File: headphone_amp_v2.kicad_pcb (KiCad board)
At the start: 2 copper layers, 94 x 73.7 mm, 73 parts, among them J1 USB_OTG, J2 HID_JMP, J3 AudioJack3_Ground, U1 PCM2707PJTG4, U2 PCM1794A, U3 TPS60501DGS, U4 OPA2134PA, U5 OPA2134PA, U6 LM2662M, Y1 12Mhz

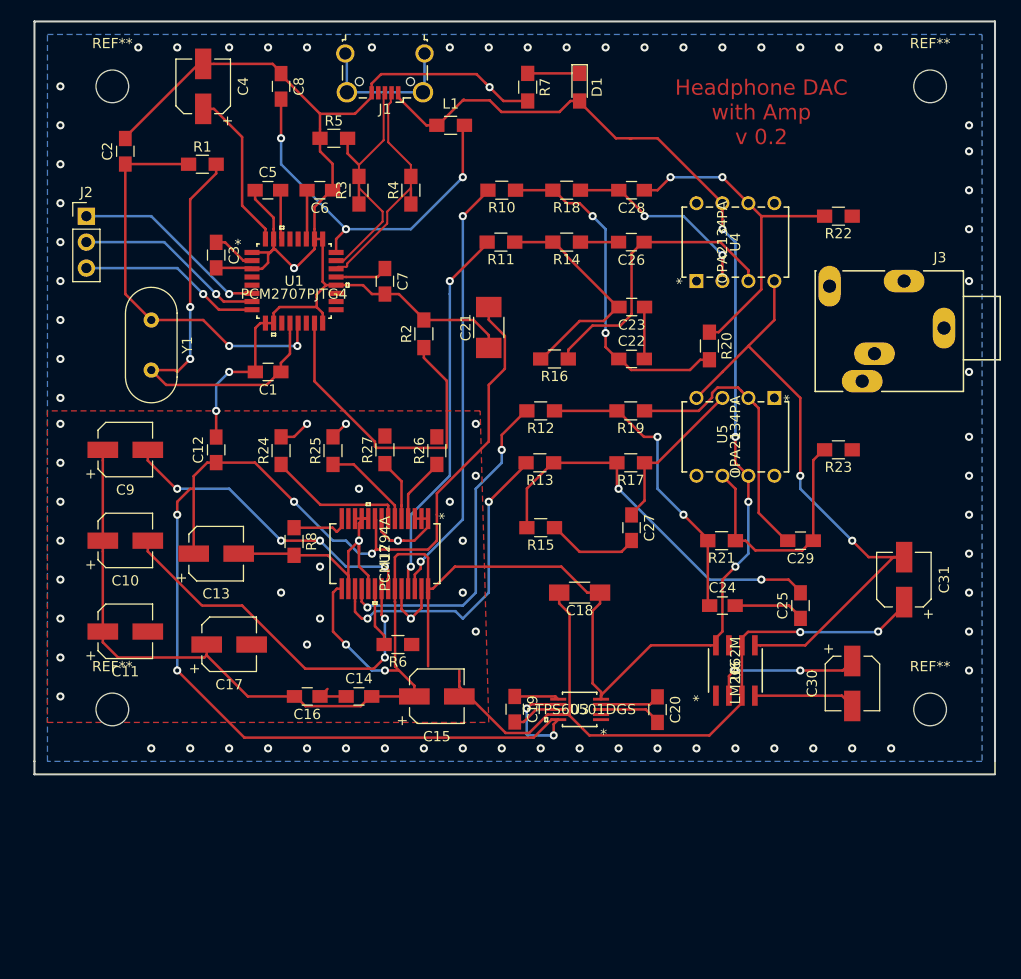
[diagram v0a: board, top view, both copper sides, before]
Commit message: updated the layout of components and rerouted the traces. The components are grouped more nicely, the board length was reduced by 5mm
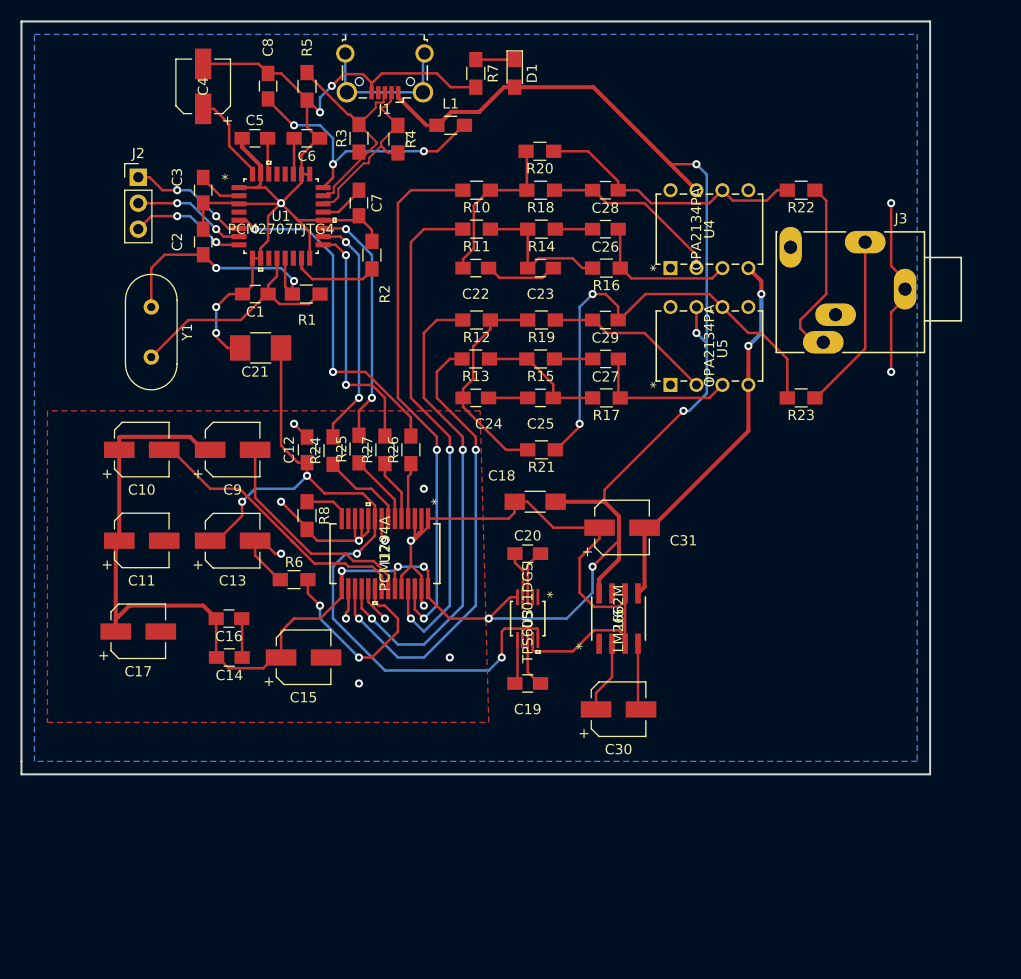
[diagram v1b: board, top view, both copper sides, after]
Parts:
- removed REF** (x4): MountingHole_3.2mm_M3, Mounting_Holes:MountingHole_3.2mm_M3
- moved C25 32.6 mm to (72.4, 49.5), turned to 0 degrees
- moved C24 31.5 mm to (66.0, 49.5)
- moved C29 28.8 mm to (78.7, 41.9)
- moved C31 28.1 mm to (80.3, 62.2), turned to 0 degrees
- moved R20 25.3 mm to (72.3, 25.4), turned to 180 degrees
- moved C30 23.0 mm to (80.0, 80.0), turned to 0 degrees
- moved C21 22.4 mm to (45.0, 44.6), turned to 0 degrees
- moved C20 19.9 mm to (71.1, 64.8), turned to 0 degrees
- moved R21 19.7 mm to (72.5, 54.6)
- moved C22 17.6 mm to (66.0, 36.8)
- moved U5 17.3 mm to (92.7, 40.6), turned to 90 degrees
- moved C27 16.7 mm to (78.7, 45.7), turned to 180 degrees
- moved R15 16.5 mm to (72.4, 45.7)
- moved R1 16.3 mm to (49.5, 39.4)
- moved C15 13.6 mm to (49.2, 74.9)
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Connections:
- net BCK renamed CLK_N
- net DATA renamed DATA_P
- net LRCK renamed DATA_N
- net SCK renamed CLK_P
- J3 pad 1: (no net) -> OUTR
- J3 pad 2: (no net) -> OUTL
- J3 pad 3: (no net) -> GND
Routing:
- net 3.3V: track 135.0 -> 75.7 mm, vias 6 -> 4
- net DATA_N: track 0.00 -> 33.5 mm, vias 0 -> 2
- net Net-(C25-Pad2): track 38.4 -> 12.4 mm, vias 2 -> 0
- net GND: track 252.4 -> 227.3 mm, vias 87 -> 19
- net -5V: track 61.8 -> 37.8 mm
- net DATA_P: track 0.00 -> 23.4 mm, vias 0 -> 2
- net Net-(R2-Pad1): track 32.3 -> 8.98 mm
- net CLK_N: track 1.80 -> 25.0 mm, vias 1 -> 2
- net 5V: track 223.9 -> 201.9 mm, vias 6 -> 8
- net Net-(C29-Pad1): track 24.7 -> 45.2 mm, vias 0 -> 2
- net CLK_P: track 3.07 -> 23.1 mm, vias 1 -> 2
- net Net-(C1-Pad1): track 43.5 -> 23.7 mm, vias 2 -> 0
- net OUTL: track 0.00 -> 17.9 mm
- net OUTR: track 0.00 -> 17.3 mm
- net Net-(C22-Pad1): track 33.4 -> 16.2 mm, vias 2 -> 0
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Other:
- board size 94 x 73.7 mm -> 88.9 x 73.7 mm
- board text removed: "Headphone DAC with Amp v 0.2"

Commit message: added mountingholes(m3)
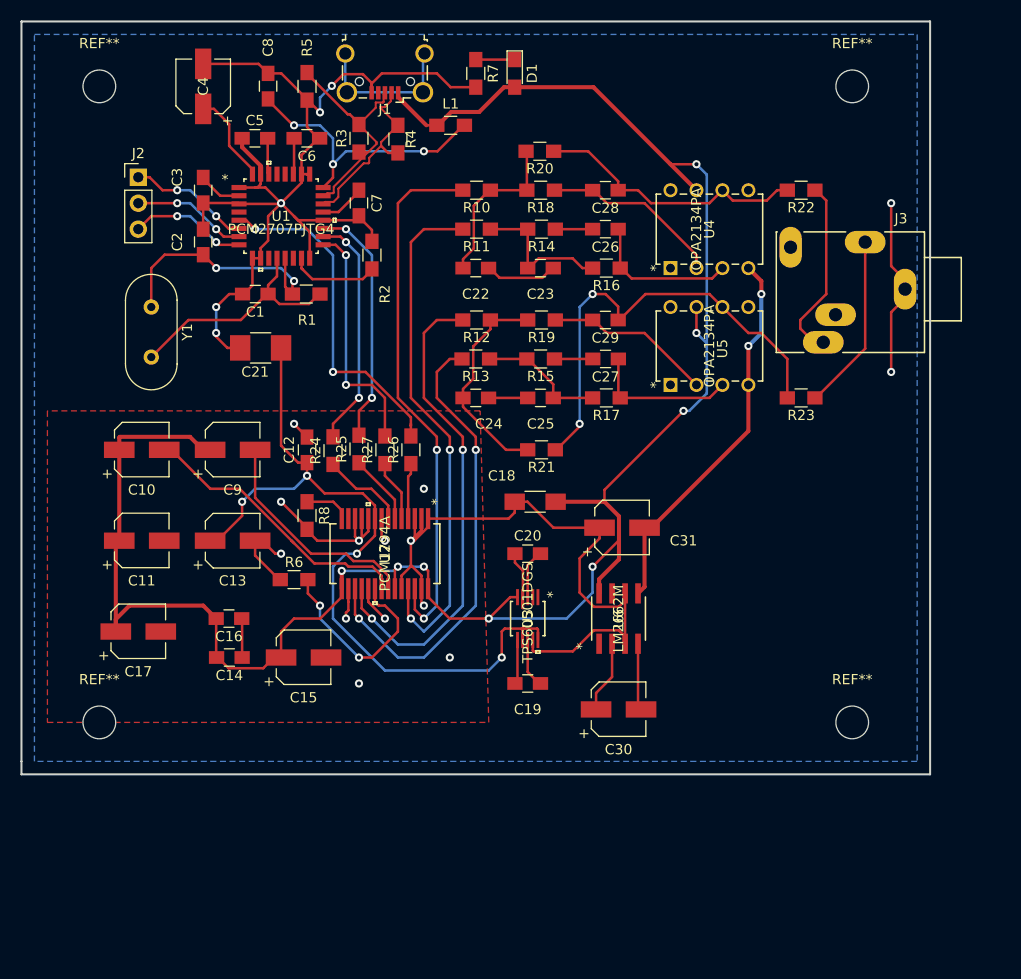
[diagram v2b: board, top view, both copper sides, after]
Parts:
- added REF**: MountingHole_3.2mm_M3, Mounting_Holes:MountingHole_3.2mm_M3, F.Cu at (29.2, 19.1)
- added REF**: MountingHole_3.2mm_M3, Mounting_Holes:MountingHole_3.2mm_M3, F.Cu at (102.9, 19.1)
- added REF**: MountingHole_3.2mm_M3, Mounting_Holes:MountingHole_3.2mm_M3, F.Cu at (102.9, 81.3)
- added REF**: MountingHole_3.2mm_M3, Mounting_Holes:MountingHole_3.2mm_M3, F.Cu at (29.2, 81.3)
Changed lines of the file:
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@@
     (tracks 664)
     (zones 0)
-    (modules 69)
+    (modules 73)
     (nets 76)
   )
@@
     )
   )
+  (module Mounting_Holes:MountingHole_3.2mm_M3 (layer F.Cu)
+    (at 29.21 19.05)
+    (descr "Mounting Hole 3.2mm, no annular, M3")
+    (tags "mounting hole 3.2mm no annular m3")
+    (attr virtual)
+    (fp_text reference REF** (at 0 -4.2) (layer F.SilkS)
+      (effects (font (size 1 1) (thickness 0.15)))
+    )
+    (fp_text value MountingHole_3.2mm_M3 (at 0 4.2) (layer F.Fab)
+      (effects (font (size 1 1) (thickness 0.15)))
+    )
+    (fp_text user %R (at 0.3 0) (layer F.Fab)
+      (effects (font (size 1 1) (thickness 0.15)))
+    )
+    (fp_circle (center 0 0) (end 3.2 0) (layer Cmts.User) (width 0.15))
+    (fp_circle (center 0 0) (end 3.45 0) (layer F.CrtYd) (width 0.05))
+    (pad 1 np_thru_hole circle (at 0 0) (size 3.2 3.2) (drill 3.2) (layers *.Cu *.Mask))
+  )
+  (module Mounting_Holes:MountingHole_3.2mm_M3 (layer F.Cu)
+    (at 102.87 19.05)
+    (descr "Mounting Hole 3.2mm, no annular, M3")
+    (tags "mounting hole 3.2mm no annular m3")
+    (attr virtual)
+    (fp_text reference REF** (at 0 -4.2) (layer F.SilkS)
+      (effects (font (size 1 1) (thickness 0.15)))
+    )
+    (fp_text value MountingHole_3.2mm_M3 (at 0 4.2) (layer F.Fab)
+      (effects (font (size 1 1) (thickness 0.15)))
+    )
+    (fp_text user %R (at 0.3 0) (layer F.Fab)
+      (effects (font (size 1 1) (thickness 0.15)))
+    )
+    (fp_circle (center 0 0) (end 3.2 0) (layer Cmts.User) (width 0.15))
+    (fp_circle (center 0 0) (end 3.45 0) (layer F.CrtYd) (width 0.05))
+    (pad 1 np_thru_hole circle (at 0 0) (size 3.2 3.2) (drill 3.2) (layers *.Cu *.Mask))
+  )
+  (module Mounting_Holes:MountingHole_3.2mm_M3 (layer F.Cu)
+    (at 102.87 81.28)
+    (descr "Mounting Hole 3.2mm, no annular, M3")
+    (tags "mounting hole 3.2mm no annular m3")
+    (attr virtual)
+    (fp_text reference REF** (at 0 -4.2) (layer F.SilkS)
+      (effects (font (size 1 1) (thickness 0.15)))
+    )
+    (fp_text value MountingHole_3.2mm_M3 (at 0 4.2) (layer F.Fab)
+      (effects (font (size 1 1) (thickness 0.15)))
+    )
+    (fp_text user %R (at 0.3 0) (layer F.Fab)
+      (effects (font (size 1 1) (thickness 0.15)))
+    )
+    (fp_circle (center 0 0) (end 3.2 0) (layer Cmts.User) (width 0.15))
+    (fp_circle (center 0 0) (end 3.45 0) (layer F.CrtYd) (width 0.05))
+    (pad 1 np_thru_hole circle (at 0 0) (size 3.2 3.2) (drill 3.2) (layers *.Cu *.Mask))
+  )
+  (module Mounting_Holes:MountingHole_3.2mm_M3 (layer F.Cu)
+    (at 29.21 81.28)
+    (descr "Mounting Hole 3.2mm, no annular, M3")
+    (tags "mounting hole 3.2mm no annular m3")
+    (attr virtual)
+    (fp_text reference REF** (at 0 -4.2) (layer F.SilkS)
+      (effects (font (size 1 1) (thickness 0.15)))
+    )
+    (fp_text value MountingHole_3.2mm_M3 (at 0 4.2) (layer F.Fab)
+      (effects (font (size 1 1) (thickness 0.15)))
+    )
+    (fp_text user %R (at 0.3 0) (layer F.Fab)
+      (effects (font (size 1 1) (thickness 0.15)))
+    )
+    (fp_circle (center 0 0) (end 3.2 0) (layer Cmts.User) (width 0.15))
+    (fp_circle (center 0 0) (end 3.45 0) (layer F.CrtYd) (width 0.05))
+    (pad 1 np_thru_hole circle (at 0 0) (size 3.2 3.2) (drill 3.2) (layers *.Cu *.Mask))
+  )
   (dimension 73.66 (width 0.3) (layer F.SilkS)

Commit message: updated the opamps and crystal to a smd version, removed ground traces in favor of vias
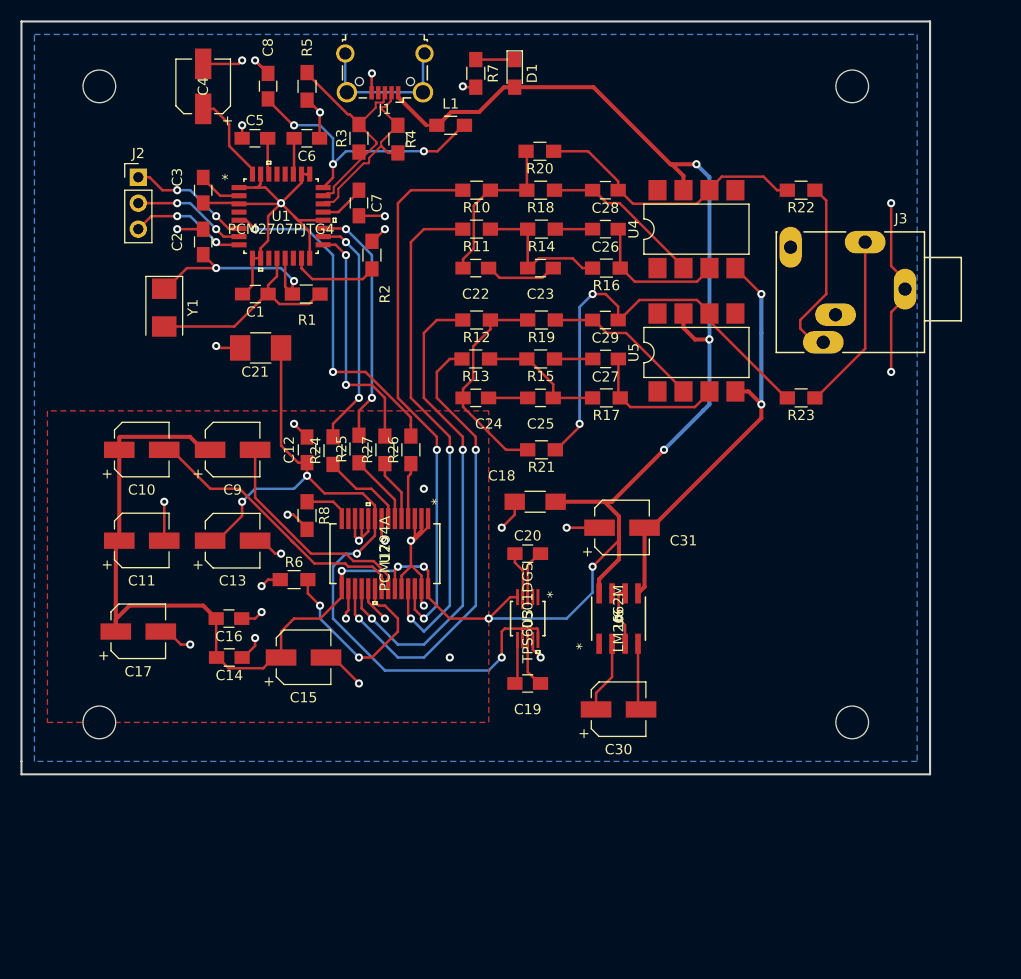
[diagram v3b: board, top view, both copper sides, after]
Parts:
- U4, U5: value OPA2134PA -> SMDIP-8_W7.62mm; footprint OPA2134PA:OPA2134PA -> Housings_DIP:SMDIP-8_W7.62mm
- Y1: footprint Crystals:Crystal_HC18-U_Vertical -> Crystals:Crystal_SMD_5032-2pin_5.0x3.2mm
- moved U5 6.75 mm to (87.6, 45.1)
- moved U4 6.35 mm to (87.6, 33.0)
- moved Y1 1.27 mm to (35.6, 40.7)
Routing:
- net GND: track 227.3 -> 157.8 mm, vias 19 -> 34
- net -5V: track 37.8 -> 41.3 mm
- net Net-(C2-Pad1): track 24.6 -> 21.0 mm
- net Net-(C1-Pad1): track 23.7 -> 21.2 mm
- net Net-(C29-Pad1): track 45.2 -> 43.0 mm
- net Net-(C28-Pad2): track 17.8 -> 15.8 mm
- net Net-(C26-Pad1): track 14.7 -> 13.8 mm
- net Net-(C29-Pad2): track 16.4 -> 15.5 mm
- net Net-(C27-Pad1): track 14.4 -> 13.7 mm

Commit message: added testpads[to be routed], updated rendered images
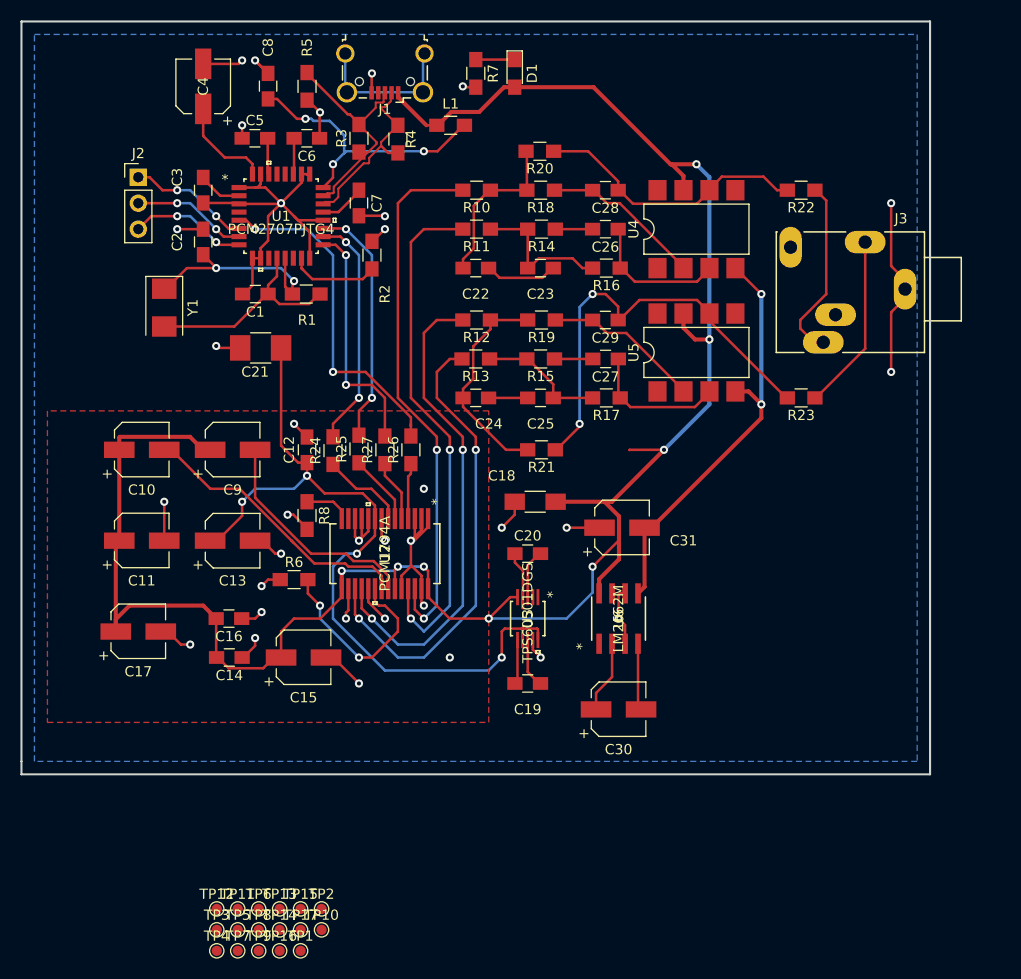
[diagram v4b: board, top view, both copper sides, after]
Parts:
- removed REF** (x4): MountingHole_3.2mm_M3, Mounting_Holes:MountingHole_3.2mm_M3
- added TP1: TestPoint_Probe, TestPoint:TestPoint_Pad_D1.0mm, F.Cu at (48.9, 103.6)
- added TP10: TestPoint_Probe, TestPoint:TestPoint_Pad_D1.0mm, F.Cu at (50.9, 101.6)
- added TP11: TestPoint_Probe, TestPoint:TestPoint_Pad_D1.0mm, F.Cu at (42.7, 99.5)
- added TP12: TestPoint_Probe, TestPoint:TestPoint_Pad_D1.0mm, F.Cu at (40.7, 99.5)
- added TP13: TestPoint_Probe, TestPoint:TestPoint_Pad_D1.0mm, F.Cu at (46.8, 99.5)
- added TP14: TestPoint_Probe, TestPoint:TestPoint_Pad_D1.0mm, F.Cu at (46.8, 101.6)
- added TP15: TestPoint_Probe, TestPoint:TestPoint_Pad_D1.0mm, F.Cu at (48.9, 99.5)
- added TP16: TestPoint_Probe, TestPoint:TestPoint_Pad_D1.0mm, F.Cu at (46.8, 103.6)
- added TP17: TestPoint_Probe, TestPoint:TestPoint_Pad_D1.0mm, F.Cu at (48.9, 101.6)
- added TP2: TestPoint_Probe, TestPoint:TestPoint_Pad_D1.0mm, F.Cu at (50.9, 99.5)
- added TP3: TestPoint_Probe, TestPoint:TestPoint_Pad_D1.0mm, F.Cu at (40.7, 101.6)
- added TP4: TestPoint_Probe, TestPoint:TestPoint_Pad_D1.0mm, F.Cu at (40.7, 103.6)
- added TP5: TestPoint_Probe, TestPoint:TestPoint_Pad_D1.0mm, F.Cu at (42.7, 101.6)
- added TP6: TestPoint_Probe, TestPoint:TestPoint_Pad_D1.0mm, F.Cu at (44.8, 99.5)
- added TP7: TestPoint_Probe, TestPoint:TestPoint_Pad_D1.0mm, F.Cu at (42.7, 103.6)
- added TP8: TestPoint_Probe, TestPoint:TestPoint_Pad_D1.0mm, F.Cu at (44.8, 101.6)
- added TP9: TestPoint_Probe, TestPoint:TestPoint_Pad_D1.0mm, F.Cu at (44.8, 103.6)
- U4, U5: value SMDIP-8_W7.62mm -> OPA2134PA
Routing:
- net 5V: track 202.0 -> 205.3 mm
- net Net-(C4-Pad1): track 9.00 -> 10.1 mm
